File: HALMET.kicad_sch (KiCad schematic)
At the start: 0 parts

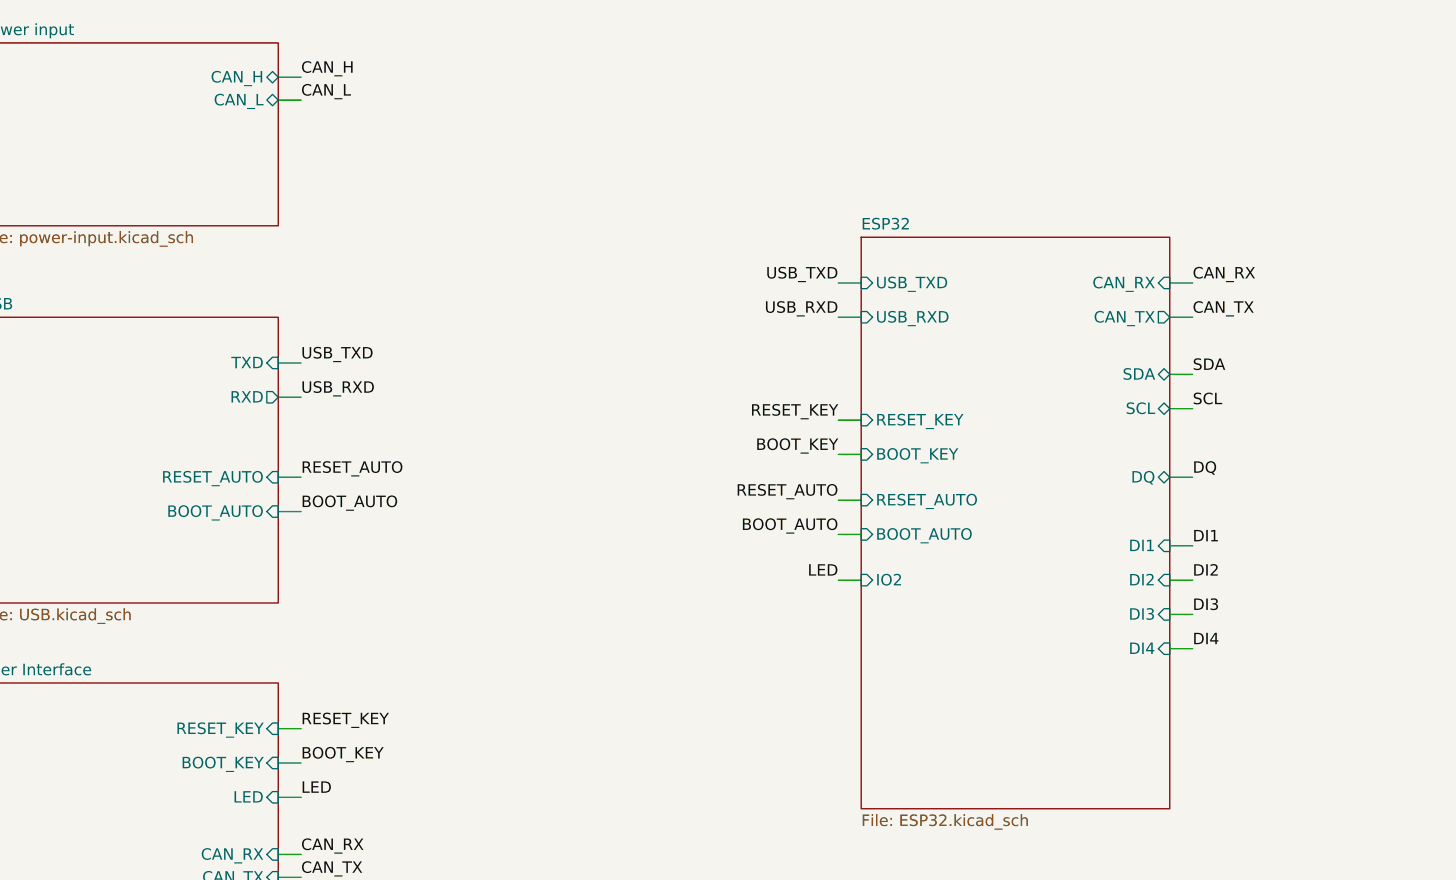
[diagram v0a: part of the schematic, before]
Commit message: Initial V1.0.0 Bluefin forked
Added ICM-42688-P 6-axis IMU
Added LM317 LDO for 6.4v or 5v MHU supply (selectable via jumper)
Added External LED's for IO2 (Pin 24) and 3.3v
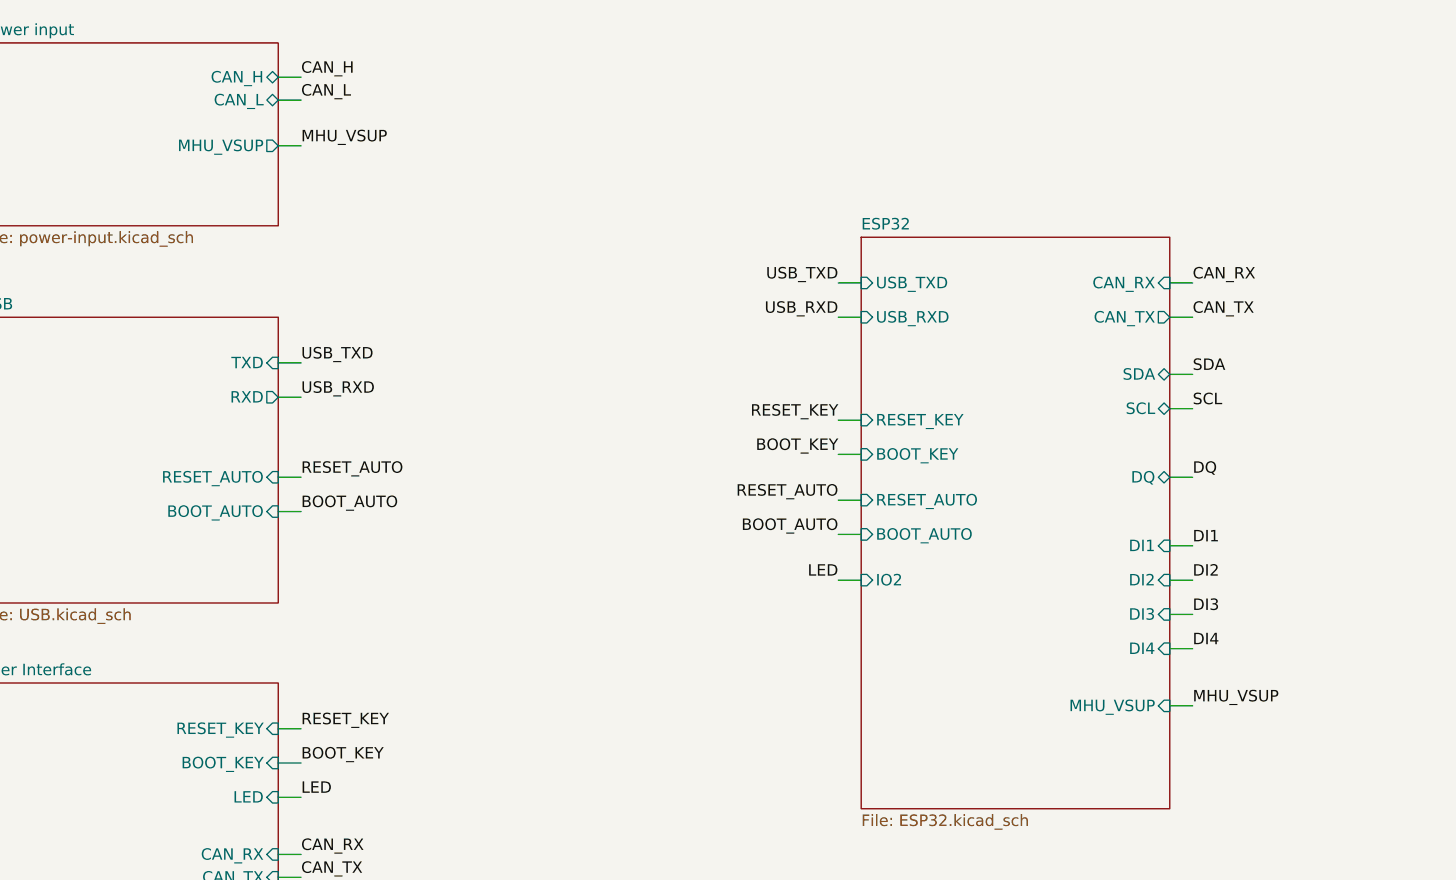
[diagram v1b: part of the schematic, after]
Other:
- sheet ESP32 ports: added MHU_VSUP; removed none
- sheet Power input ports: added MHU_VSUP; removed none
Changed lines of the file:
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@@
+	(wire
+		(pts
+			(xy 57.15 35.56) (xy 59.69 35.56)
+		)
+		(stroke
+			(width 0)
+			(type default)
+		)
+	)
 	(wire
 		(pts
@@
 		(pts
 			(xy 233.68 39.37) (xy 236.22 39.37)
+		)
+		(stroke
+			(width 0)
+			(type default)
+		)
+	)
+	(wire
+		(pts
+			(xy 156.21 97.79) (xy 158.75 97.79)
 		)
 		(stroke
@@
 		)
 	)
+	(label "MHU_VSUP"
+		(at 59.69 35.56 0)
+		(effects
+			(font
+				(size 1.27 1.27)
+			)
+			(justify left bottom)
+		)
+	)
 	(label "LED"
 		(at 59.69 107.95 0)
@@
 	(label "CAN_L"
 		(at 59.69 30.48 0)
+		(effects
+			(font
+				(size 1.27 1.27)
+			)
+			(justify left bottom)
+		)
+	)
+	(label "MHU_VSUP"
+		(at 158.75 97.79 0)
 		(effects
 			(font
@@
 			)
 		)
+		(pin "MHU_VSUP" output
+			(at 57.15 35.56 0)
+			(effects
+				(font
+					(size 1.27 1.27)
+				)
+				(justify right)
+			)
+		)
 		(instances
 			(project "HALMET"
@@
 			(effects
 				(font
+					(size 1.27 1.27)
+				)
+				(justify right)
+			)
+		)
+		(pin "MHU_VSUP" input
+			(at 156.21 97.79 0)
+			(effects
+				(font

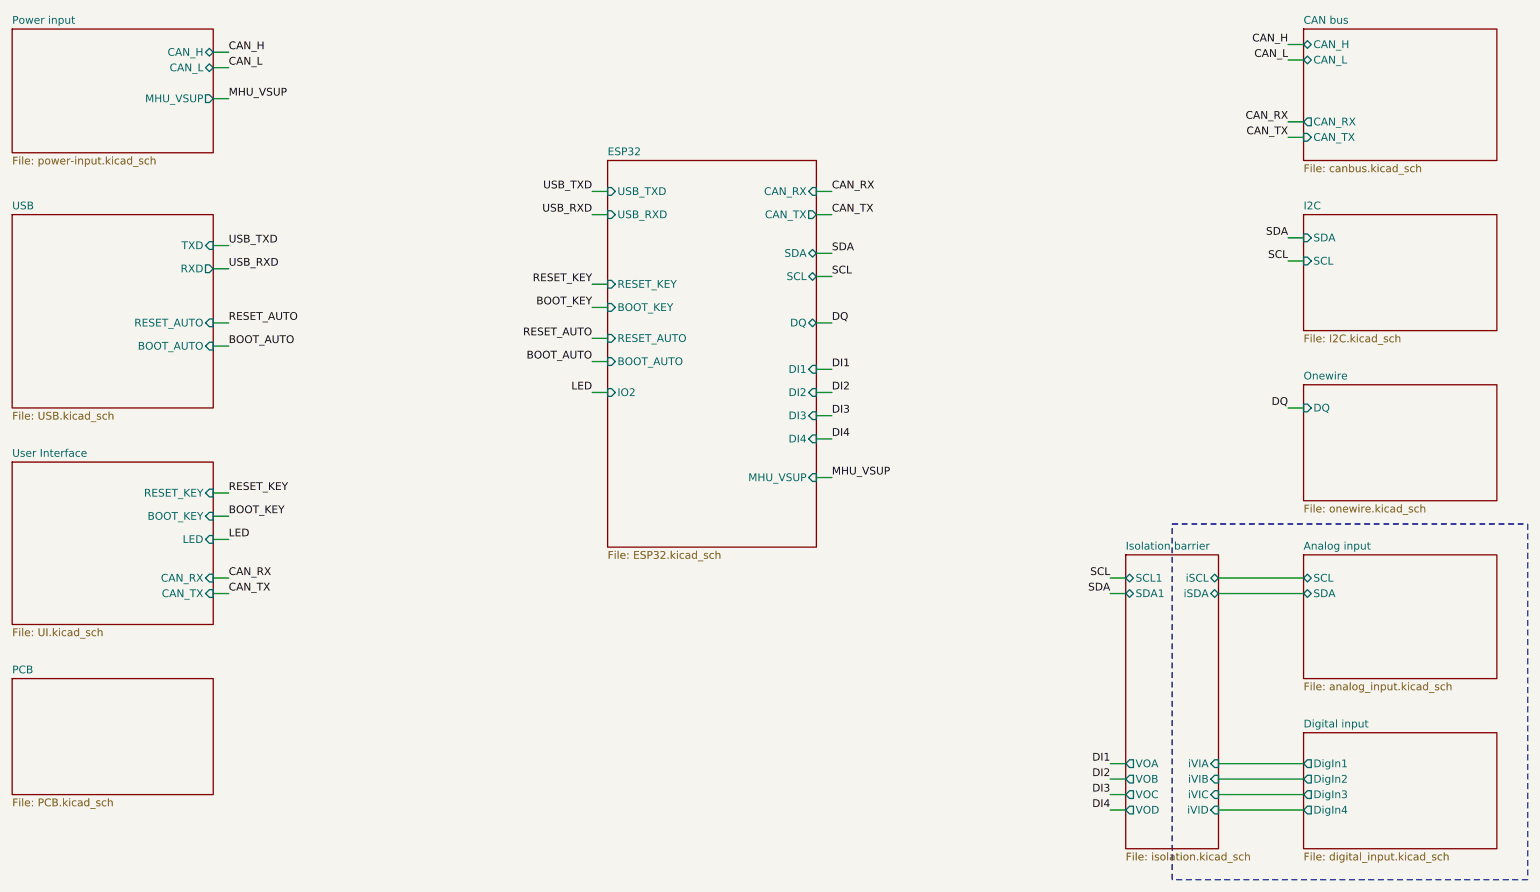
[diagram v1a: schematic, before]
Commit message: Added RS485/RS233 (NMEA 01830) chip
Added SP3485EN RS485 bi-directional driver with a GPIO toggle for changing input - output direction.

Connected to GPIO pin header
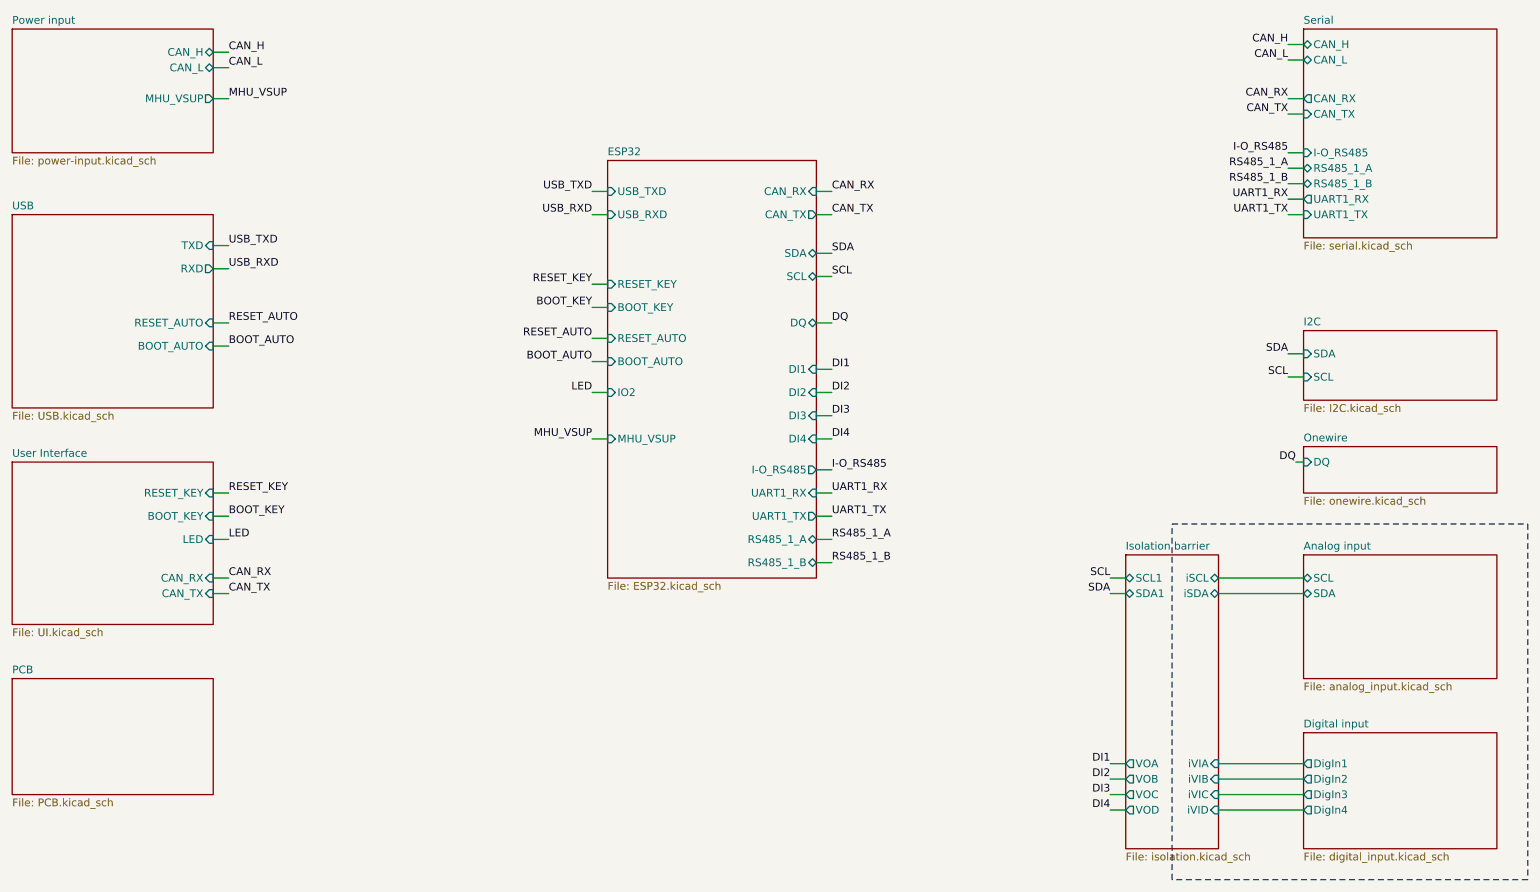
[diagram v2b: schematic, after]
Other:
- sheet CAN bus renamed Serial
- sheet ESP32 ports: added I-O_RS485, RS485_1_A, RS485_1_B, UART1_RX, UART1_TX; removed none
- sheet Serial: file canbus.kicad_sch -> serial.kicad_sch
- sheet Serial ports: added I-O_RS485, RS485_1_A, RS485_1_B, UART1_RX, UART1_TX; removed none

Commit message: Changed to ESP32-S3-WROOM-1U
Added ESP32-S3-WROOM-1U-N16R2  and updated all routing and pin assignments.

Added USB-OTG connected via JST-PH
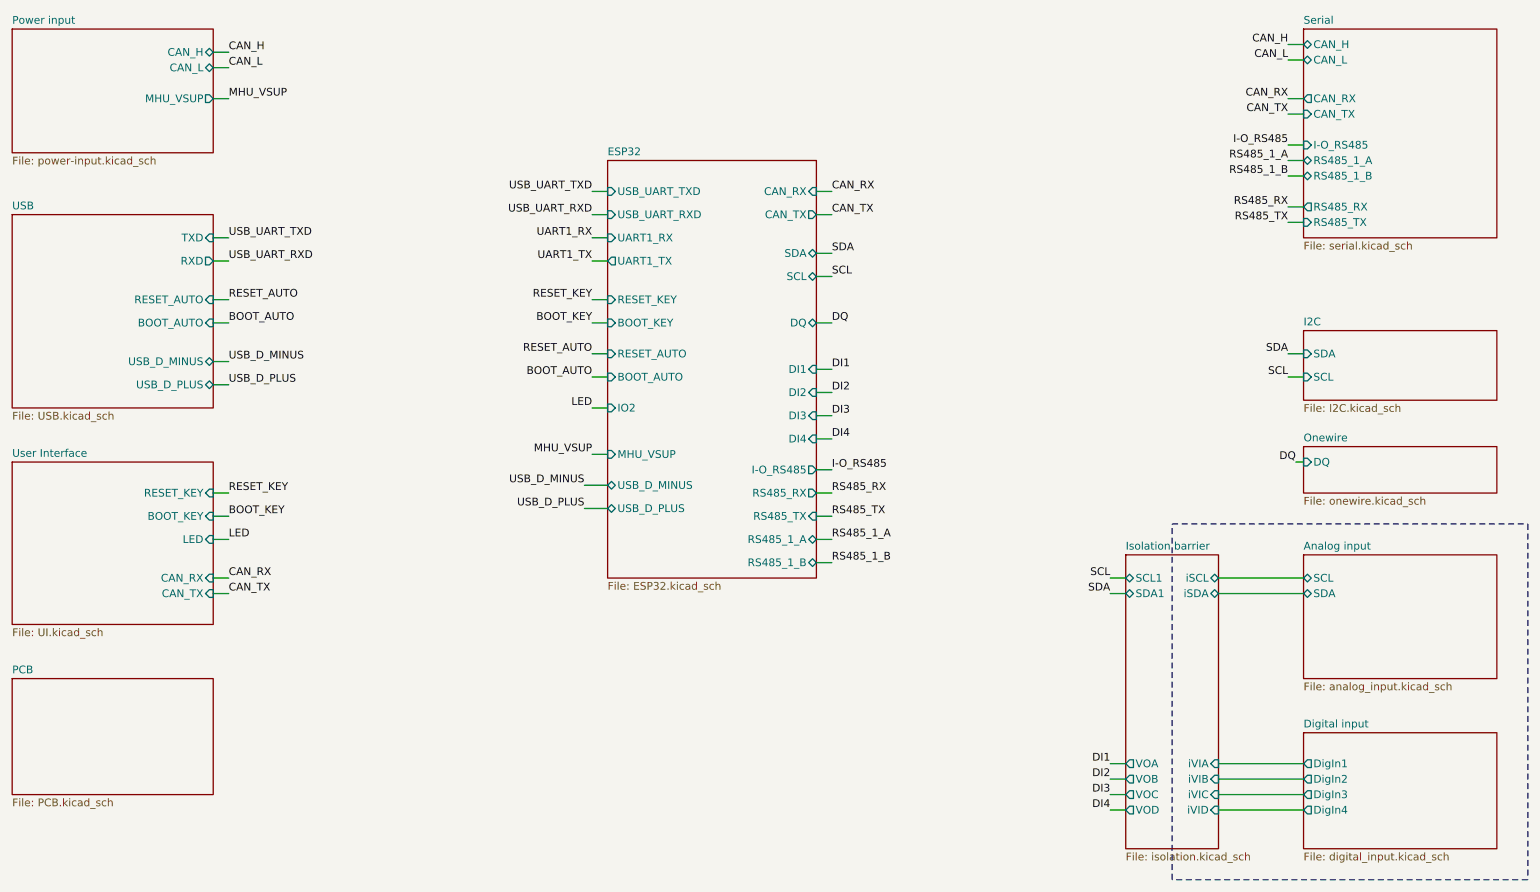
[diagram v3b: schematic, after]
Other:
- sheet ESP32 ports: added RS485_RX, RS485_TX, USB_D_MINUS, USB_D_PLUS, USB_UART_RXD, USB_UART_TXD; removed USB_RXD, USB_TXD
- sheet Serial ports: added RS485_RX, RS485_TX; removed UART1_RX, UART1_TX
- sheet USB ports: added USB_D_MINUS, USB_D_PLUS; removed none

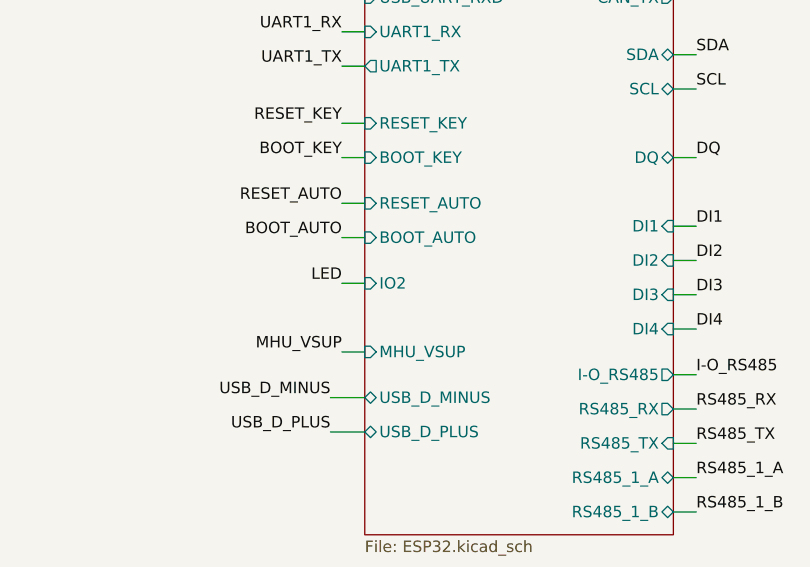
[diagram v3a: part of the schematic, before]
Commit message: Silkscreen updates
Back silkscreen bough up-to-date with GPIO pin changes
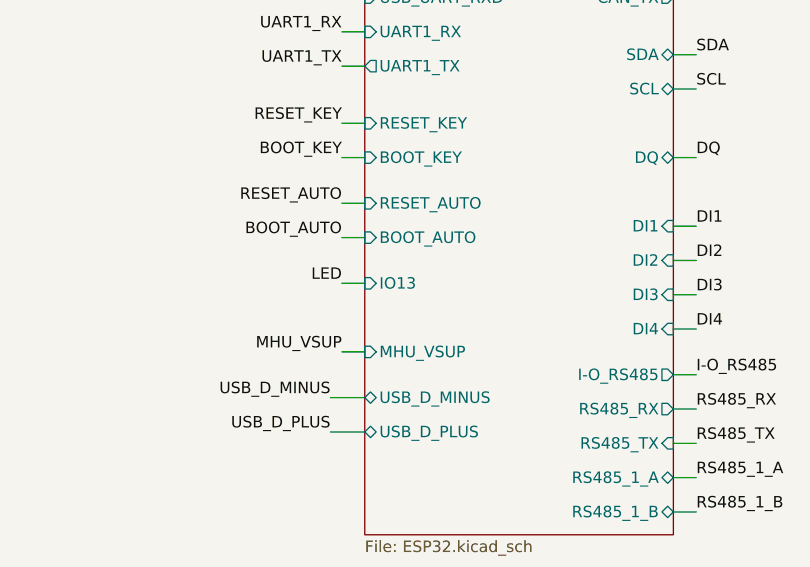
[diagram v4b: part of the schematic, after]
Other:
- sheet ESP32 ports: added IO13; removed IO2
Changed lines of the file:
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@@
 			)
 		)
-		(pin "IO2" input
+		(pin "IO13" input
 			(at 121.92 86.36 180)
 			(effects
